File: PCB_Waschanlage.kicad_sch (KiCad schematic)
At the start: 81 parts, among them J1 DSUB_1, J10 JMPR_LED_BTN_Sensor_1, J11 JMPR_LED_BTN_Sensor_4, J12 Conn_LED_Error, J13 Conn_LED_MainWash, J14 Conn_BTN_Start, J15 Conn_BTN_Basic, J16 Conn_LED_Motor, J17 Conn_LED_Red, J18 Conn_BTN_Sensor_1, J19 Conn_BTN_Sensor_4, J2 DSUB_2, J20 JMPR_LED_PreWash, J21 JMPR_LED_Start, J22 JMPR_LED_Basic, J23 JMPR_LED_BTN_On_Off, J24 JMPR_LED_BTN_Special, J25 JMPR_LED_Green, J26 JMPR_LED_BTN_Sensor_2, J27 JMPR_LED_BTN_Sensor_5, J28 Conn_LED_PreWash, J29 Conn_LED_Start, J3 Conn_Fuse, J30 Conn_LED_Basic, J31 Conn_BTN_On_Off, J32 Conn_BTN_Special, J33 Conn_LED_Green, J34 Conn_BTN_Sensor_2, J35 Conn_BTN_Sensor_5, J36 JMPR_LED_Special, J37 JMPR_LED_Care, J38 JMPR_LED_Underbody, J39 JMPR_LED_BTN_EmergencyOff, J4 JMPR_LED_Error, J40 JMPR_LED_BTN_Premium, J41 JMPR_LED_BTN_Sensor_3, J42 Conn_LED_Special, J43 Conn_LED_Care, J44 Conn_LED_Underbody, J45 Conn_BTN_EmergencyOff, J46 Conn_BTN_Premium, J47 Conn_BTN_Sensor_3, J48 JMPR_LED_Rims, J49 JMPR_LED_Premium, J5 JMPR_LED_MainWash, J50 JMPR_LED_Dry, J51 Conn_LED_Rims, J52 Conn_LED_Premium, J53 Conn_LED_Dry, J54 Conn_AdditionalPins_1, J55 Conn_AdditionalPins_2, J56 Conn_AdditionalPins_3, J6 JMPR_LED_BTN_Start, J7 JMPR_LED_BTN_Basic, J8 JMPR_LED_Motor, J9 JMPR_LED_Red

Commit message: Changed Connectors and Rerouting
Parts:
- J1: footprint Connector_Dsub:DSUB-25_Pins_Horizontal_P2.77x2.84mm_EdgePinOffset9.90mm_Housed_MountingHolesOffset11.32mm -> Connector_FFC-FPC:Hirose_FH12-25S-0.5SH_1x25-1MP_P0.50mm_Horizontal
- J14, J15, J18, J19, J31, J32, J34, J35, J45, J46, J47: footprint TerminalBlock:TerminalBlock_MaiXu_MX126-5.0-04P_1x04_P5.00mm -> TBL002A-350-04GY-2GY:CUI_TBL002A-350-04GY-2GY
- J28: footprint TerminalBlock:TerminalBlock_MaiXu_MX126-5.0-02P_1x02_P5.00mm -> TBL002A-350-02GY-2GY:CUI_TBL002A-350-02GY-2GY

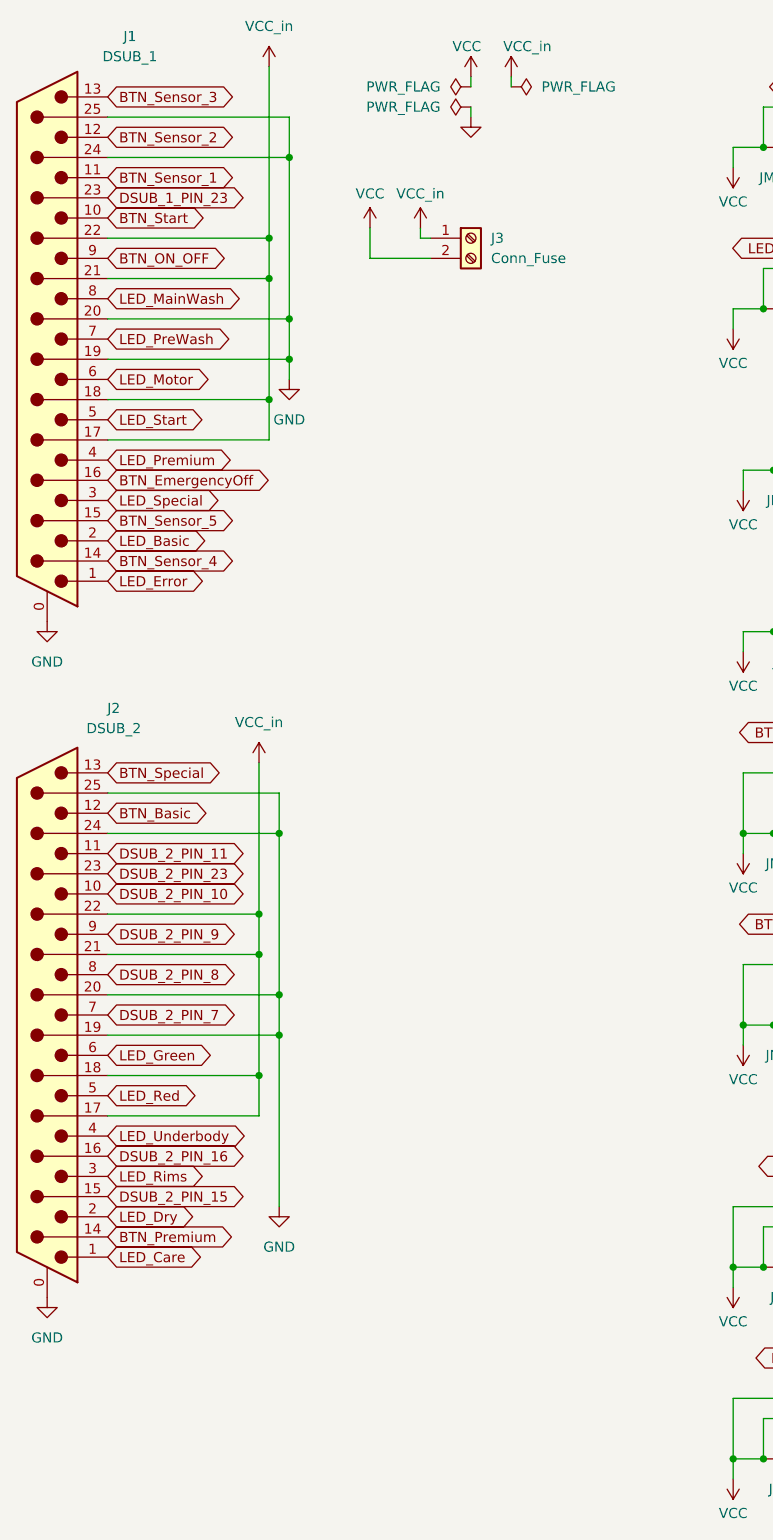
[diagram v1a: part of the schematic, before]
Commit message: Added new connectors on the PCB
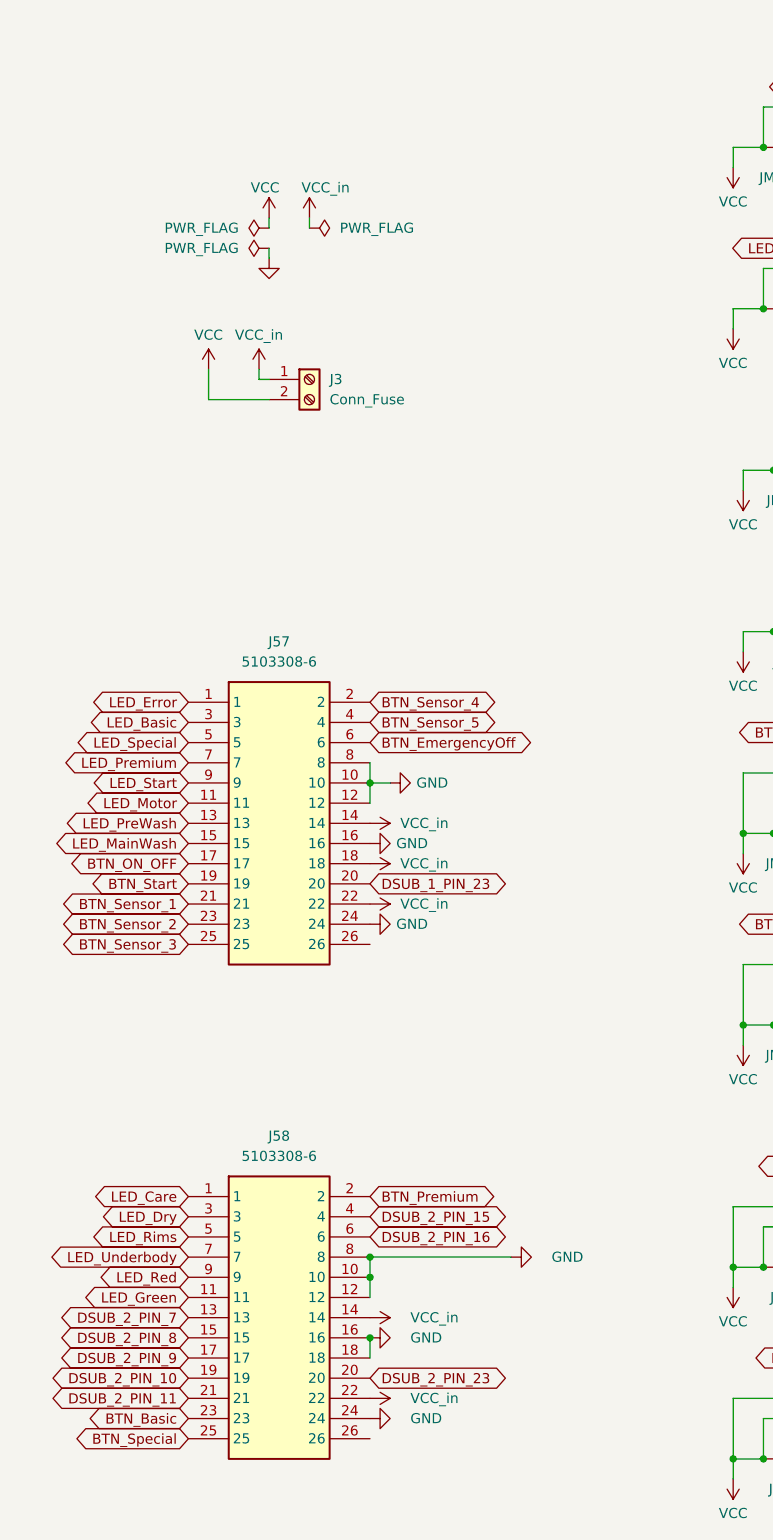
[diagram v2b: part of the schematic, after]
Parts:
- removed J1: DSUB_1, Connector_FFC-FPC:Hirose_FH12-25S-0.5SH_1x25-1MP_P0.50mm_Horizontal, symbol Connector:DB25_Pins_MountingHoles
- removed J2: DSUB_2, Connector_Dsub:DSUB-25_Pins_Horizontal_P2.77x2.84mm_EdgePinOffset9.90mm_Housed_MountingHolesOffset11.32mm, symbol Connector:DB25_Pins_MountingHoles
- added J57, J58: 5103308-6, project:SHDR26W66P254_2X13_4051X914X986P, symbol TE 5103308-6:5103308-6
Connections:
- net BTN_Basic: now also J58.23
- net BTN_EmergencyOff: now also J57.6
- net BTN_ON_OFF: now also J57.17
- net BTN_Premium: now also J58.2
- net BTN_Sensor_1: now also J57.21
- net BTN_Sensor_2: now also J57.23
- net BTN_Sensor_3: now also J57.25
- net BTN_Sensor_4: now also J57.2
- net BTN_Sensor_5: now also J57.4
- net BTN_Special: now also J58.25
- net BTN_Start: now also J57.19
- net DSUB_1_PIN_23: now also J57.20
- net DSUB_2_PIN_10: now also J58.19
- net DSUB_2_PIN_11: now also J58.21
- net DSUB_2_PIN_15: now also J58.4
- net DSUB_2_PIN_16: now also J58.6
- net DSUB_2_PIN_23: now also J58.20
- net DSUB_2_PIN_7: now also J58.13
- net DSUB_2_PIN_8: now also J58.15
- net DSUB_2_PIN_9: now also J58.17
- net GND: now also J57.10, J57.12, J57.16, J57.24, J57.8, J58.10, J58.12, J58.16, J58.18, J58.24, J58.8
- net LED_Basic: now also J57.3
- net LED_Care: now also J58.1
- net LED_Dry: now also J58.3
- net LED_Error: now also J57.1
- net LED_Green: now also J58.11
- net LED_MainWash: now also J57.15
- net LED_Motor: now also J57.11
- net LED_PreWash: now also J57.13
- net LED_Premium: now also J57.7
- net LED_Red: now also J58.9
- net LED_Rims: now also J58.5
- net LED_Special: now also J57.5
- net LED_Start: now also J57.9
- net LED_Underbody: now also J58.7
- net VCC_in: now also J57.14, J57.18, J57.22, J58.14, J58.22
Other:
- moved on the sheet: J3

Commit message: Routing fimished
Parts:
- J54, J55, J56: footprint TerminalBlock:TerminalBlock_MaiXu_MX126-5.0-04P_1x04_P5.00mm -> TBL002A-350-04GY-2GY:CUI_TBL002A-350-04GY-2GY
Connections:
- net DSUB_2_PIN_10: now also J55.4 (Pin_4); no longer J56.1 (Pin_1)
- net DSUB_2_PIN_11: now also J56.1 (Pin_1); no longer J55.4 (Pin_4)
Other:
- note added: "Spare I/O"
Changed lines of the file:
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@@
 	(generator_version "10.0")
 	(paper "A3")
+	(rectangle
+		(start 318.77 22.86)
+		(end 372.11 68.58)
+		(stroke
+			(width 0)
+			(type default)
+		)
+		(fill
+			(type none)
+		)
+	)
+	(text "Spare I/O"
+		(exclude_from_sim no)
+		(at 324.612 25.146 0)
+		(effects
+			(font
+				(size 1.27 1.27)
+			)
+		)
+	)
 	(junction
 		(at 208.28 116.84)
@@
 	(wire
 		(pts
-			(xy 320.04 41.91) (xy 320.04 38.1)
+			(xy 336.55 36.83) (xy 336.55 38.1)
 		)
 		(stroke
@@
 	(wire
 		(pts
-			(xy 320.04 38.1) (xy 340.36 38.1)
+			(xy 336.55 38.1) (xy 340.36 38.1)
 		)
 		(stroke
@@
 		)
 	)
+	(global_label "DSUB_2_PIN_11"
+		(shape bidirectional)
+		(at 340.36 55.88 180)
+		(fields_autoplaced yes)
+		(effects
+			(font
+				(size 1.27 1.27)
+			)
+			(justify right)
+		)
+		(property "Intersheetrefs" "${INTERSHEET_REFS}"
+			(at 321.4469 55.88 0)
+			(hide yes)
+			(show_name no)
+			(do_not_autoplace no)
+			(effects
+				(font
+					(size 1.27 1.27)
+				)
+				(justify right)
+			)
+		)
+	)
 	(global_label "DSUB_2_PIN_8"
 		(shape bidirectional)
@@
 		)
 	)
-	(global_label "DSUB_2_PIN_10"
-		(shape bidirectional)
-		(at 340.36 55.88 180)
-		(fields_autoplaced yes)
-		(effects
-			(font
-				(size 1.27 1.27)
-			)
-			(justify right)
-		)
-		(property "Intersheetrefs" "${INTERSHEET_REFS}"
-			(at 321.4469 55.88 0)
-			(hide yes)
-			(show_name no)
-			(do_not_autoplace no)
-			(effects
-				(font
-					(size 1.27 1.27)
-				)
-				(justify right)
-			)
-		)
-	)
 	(global_label "DSUB_2_PIN_16"
 		(shape bidirectional)
@@
 		)
 	)
-	(global_label "LED_Basic"
+	(global_label "DSUB_2_PIN_10"
 		(shape bidirectional)
-		(at 40.64 102.87 180)
+		(at 340.36 52.07 180)
 		(fields_autoplaced yes)
 		(effects
@@
 		)
 		(property "Intersheetrefs" "${INTERSHEET_REFS}"
-			(at 26.9883 102.87 0)
+			(at 321.4469 52.07 0)
 			(hide yes)
 			(show_name no)
@@
 		)
 	)
-	(global_label "BTN_Basic"
+	(global_label "LED_Basic"
 		(shape bidirectional)
-		(at 40.64 190.5 180)
+		(at 40.64 102.87 180)
 		(fields_autoplaced yes)
 		(effects
@@
 		)
 		(property "Intersheetrefs" "${INTERSHEET_REFS}"
-			(at 26.8673 190.5 0)
+			(at 26.9883 102.87 0)
 			(hide yes)
 			(show_name no)
@@
 		)
 	)
-	(global_label "LED_Basic"
+	(global_label "BTN_Basic"
 		(shape bidirectional)
-		(at 172.72 22.86 180)
+		(at 40.64 190.5 180)
 		(fields_autoplaced yes)
 		(effects
@@
 		)
 		(property "Intersheetrefs" "${INTERSHEET_REFS}"
-			(at 159.0683 22.86 0)
+			(at 26.8673 190.5 0)
 			(hide yes)
 			(show_name no)
@@
 		)
 	)
-	(global_label "DSUB_2_PIN_7"
+	(global_label "LED_Basic"
 		(shape bidirectional)
-		(at 340.36 63.5 180)
+		(at 172.72 22.86 180)
 		(fields_autoplaced yes)
 		(effects
@@
 		)
 		(property "Intersheetrefs" "${INTERSHEET_REFS}"
-			(at 322.6564 63.5 0)
+			(at 159.0683 22.86 0)
 			(hide yes)
 			(show_name no)
@@
 		)
 	)
-	(global_label "LED_Care"
+	(global_label "DSUB_2_PIN_7"
 		(shape bidirectional)
-		(at 214.63 43.18 180)
+		(at 340.36 63.5 180)
 		(fields_autoplaced yes)
 		(effects
@@
 		)
 		(property "Intersheetrefs" "${INTERSHEET_REFS}"
-			(at 201.825 43.18 0)
+			(at 322.6564 63.5 0)
 			(hide yes)
 			(show_name no)
@@
 		)
 	)
-	(global_label "DSUB_2_PIN_11"
+	(global_label "LED_Care"
 		(shape bidirectional)
-		(at 340.36 52.07 180)
+		(at 214.63 43.18 180)
 		(fields_autoplaced yes)
 		(effects
@@
 		)
 		(property "Intersheetrefs" "${INTERSHEET_REFS}"
-			(at 321.4469 52.07 0)
+			(at 201.825 43.18 0)
 			(hide yes)
 			(show_name no)
@@
 			)
 		)
-		(property "Footprint" "TerminalBlock:TerminalBlock_MaiXu_MX126-5.0-04P_1x04_P5.00mm"
+		(property "Footprint" "TBL002A-350-04GY-2GY:CUI_TBL002A-350-04GY-2GY"
 			(at 345.44 35.56 0)
 			(hide yes)
@@
 			)
 		)
-		(property "Footprint" "TerminalBlock:TerminalBlock_MaiXu_MX126-5.0-04P_1x04_P5.00mm"
+		(property "Footprint" "TBL002A-350-04GY-2GY:CUI_TBL002A-350-04GY-2GY"
 			(at 345.44 58.42 0)
 			(hide yes)
@@
 			)
 		)
-		(property "Footprint" "TerminalBlock:TerminalBlock_MaiXu_MX126-5.0-04P_1x04_P5.00mm"
+		(property "Footprint" "TBL002A-350-04GY-2GY:CUI_TBL002A-350-04GY-2GY"
 			(at 345.44 46.99 0)
 			(hide yes)
@@
 	(symbol
 		(lib_id "power:GND")
-		(at 320.04 41.91 0)
+		(at 336.55 36.83 270)
 		(unit 1)
 		(body_style 1)
@@
 		(dnp no)
 		(property "Reference" "#PWR037"
-			(at 320.04 48.26 0)
+			(at 330.2 36.83 0)
 			(hide yes)
 			(show_name no)
@@
 		)
 		(property "Value" "GND"
-			(at 317.754 42.164 0)
+			(at 331.216 36.83 90)
 			(show_name no)
 			(do_not_autoplace no)
@@
 		)
 		(property "Footprint" ""
-			(at 320.04 41.91 0)
+			(at 336.55 36.83 0)
 			(hide yes)
 			(show_name no)
@@
 		)
 		(property "Datasheet" ""
-			(at 320.04 41.91 0)
+			(at 336.55 36.83 0)
 			(hide yes)
 			(show_name no)
@@
 		)
 		(property "Description" "Power symbol creates a global label with name \"GND\" , ground"
-			(at 320.04 41.91 0)
+			(at 336.55 36.83 0)
 			(hide yes)
 			(show_name no)
@@
 		(in_pos_files yes)
 		(dnp no)
-		(fields_autoplaced yes)
 		(property "Reference" "#PWR038"
 			(at 337.82 35.56 0)
@@
 		)
 		(property "Value" "VCC"
-			(at 337.82 26.67 0)
+			(at 337.82 27.178 0)
 			(show_name no)
 			(do_not_autoplace no)

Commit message: Silkscreen added
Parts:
- J20: footprint TBL002A-350-02GY-2GY:CUI_TBL002A-350-02GY-2GY -> Connector_PinHeader_2.54mm:PinHeader_1x02_P2.54mm_Vertical
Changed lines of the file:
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@@
 			)
 		)
-		(property "Footprint" "TBL002A-350-02GY-2GY:CUI_TBL002A-350-02GY-2GY"
+		(property "Footprint" "Connector_PinHeader_2.54mm:PinHeader_1x02_P2.54mm_Vertical"
 			(at 162.56 50.8 0)
 			(hide yes)

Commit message: all done
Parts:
- added H1, H2, H3, H4, H5, H6: MountingHole, MountingHole:MountingHole_4.3mm_M4, symbol Mechanical:MountingHole
